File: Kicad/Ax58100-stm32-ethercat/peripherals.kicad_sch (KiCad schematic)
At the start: 32 parts, among them J1 Out_opt, J15 Conn_01x04, J16 Conn_01x02, J17 Conn_01x04, J18 Conn_01x08, J3 In_opt1, J5 In_opt2, J6 DAC, U6 TLP292-4, U7 TLP291-4, U8 TLP292-4

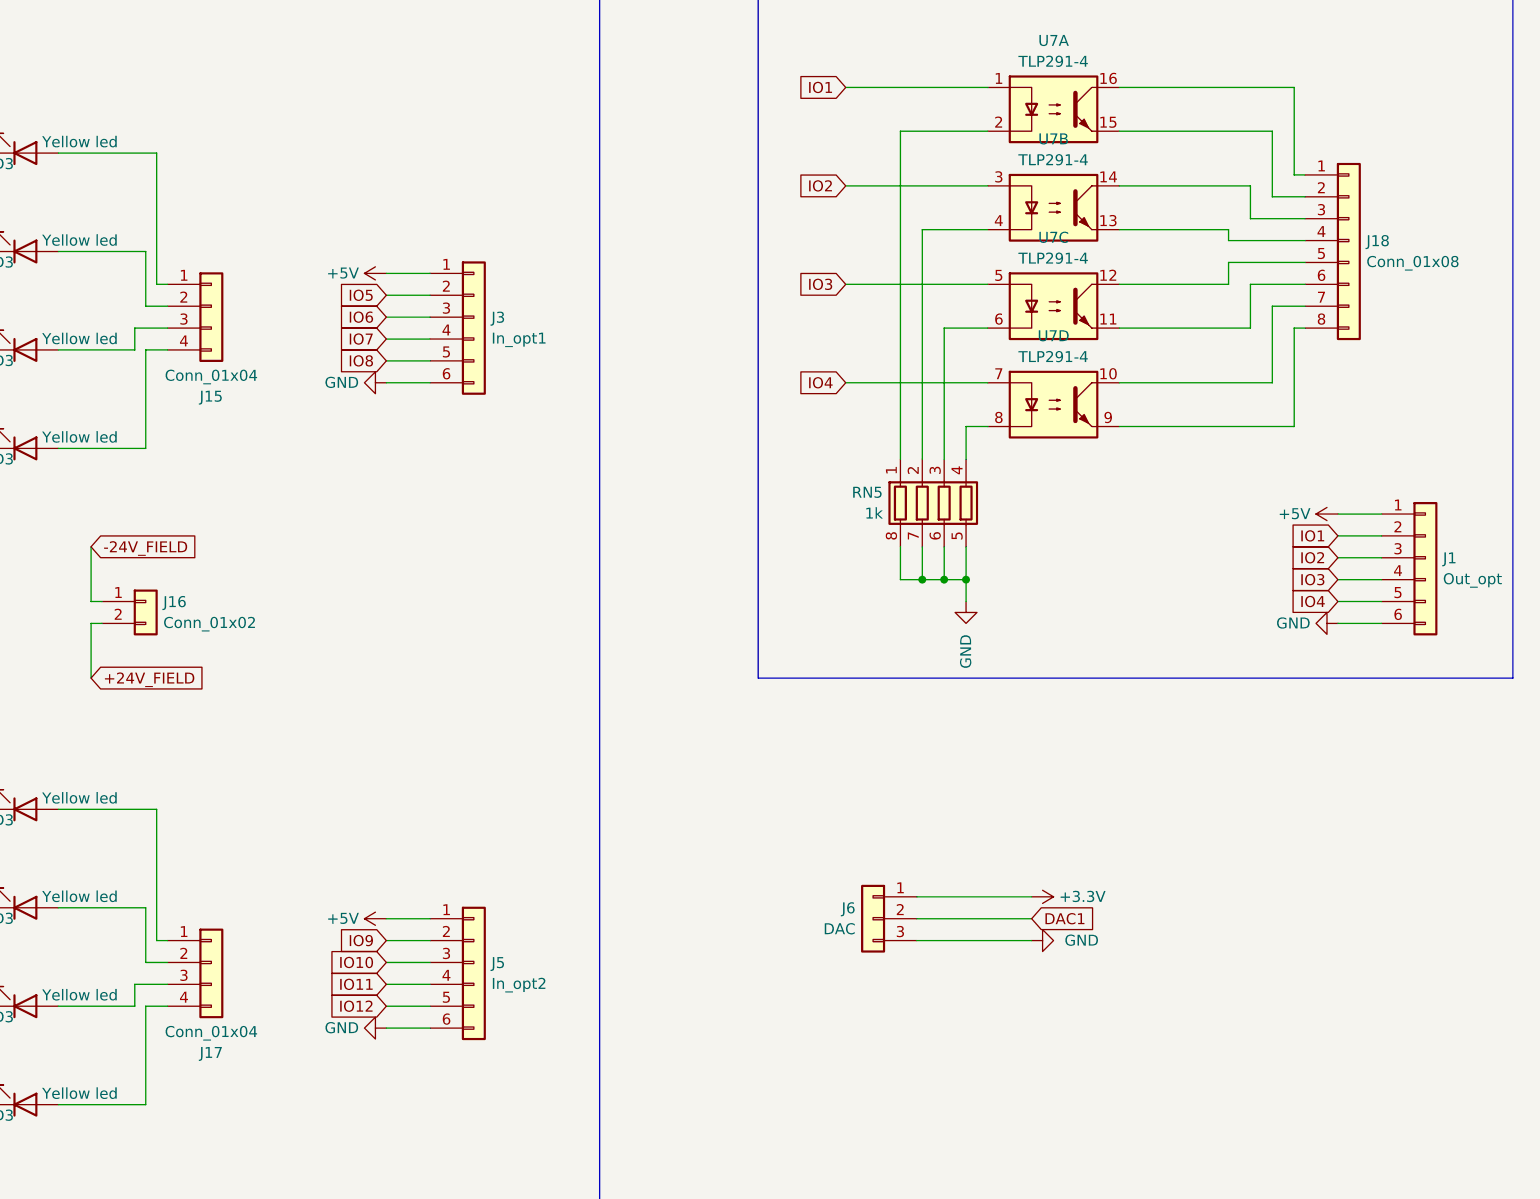
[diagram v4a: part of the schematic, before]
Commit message: Assigned footprints
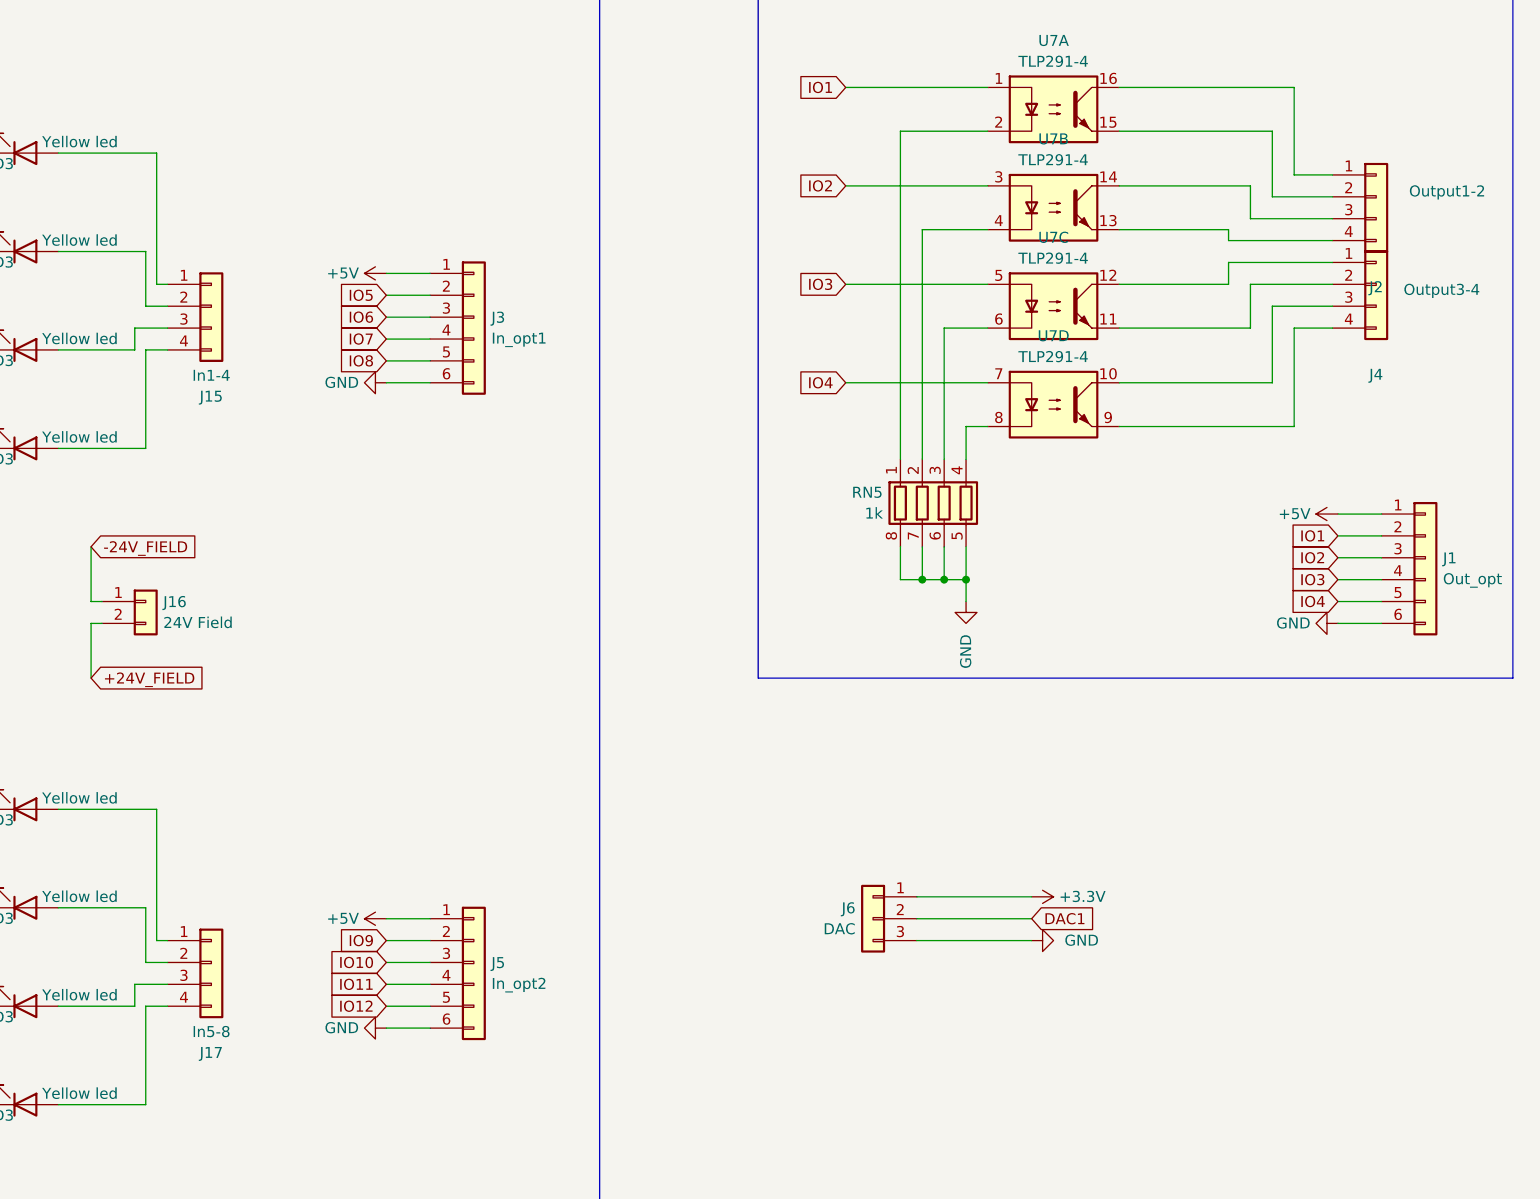
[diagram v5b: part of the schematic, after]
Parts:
- removed J18: Conn_01x08, symbol Connector_Generic:Conn_01x08
- added J2: Output1-2, TerminalBlock:TerminalBlock_bornier-4_P5.08mm, symbol Connector_Generic:Conn_01x04
- added J4: Output3-4, TerminalBlock:TerminalBlock_bornier-4_P5.08mm, symbol Connector_Generic:Conn_01x04
- J1, J3, J5: footprint (none) -> Connector_JST:JST_XH_B6B-XH-A_1x06_P2.50mm_Vertical
- J15: value Conn_01x04 -> In1-4; footprint (none) -> TerminalBlock:TerminalBlock_bornier-4_P5.08mm
- J16: value Conn_01x02 -> 24V Field; footprint (none) -> TerminalBlock:TerminalBlock_bornier-2_P5.08mm
- J17: value Conn_01x04 -> In5-8; footprint (none) -> TerminalBlock:TerminalBlock_bornier-4_P5.08mm
- J6: footprint (none) -> TerminalBlock:TerminalBlock_bornier-3_P5.08mm
- RN1, RN2, RN3, RN4, RN5: footprint (none) -> Resistor_SMD:R_Array_Convex_4x0603
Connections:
- net at U7.10: now also J4.3 (Pin_3)
- net at U7.9: now also J4.4 (Pin_4)
- net at U7.15: now also J2.2 (Pin_2)
- net at U7.16: now also J2.1 (Pin_1)
- net at U7.14: now also J2.3 (Pin_3)
- net at U7.13: now also J2.4 (Pin_4)
- net at U7.12: now also J4.1 (Pin_1)
- net at U7.11: now also J4.2 (Pin_2)
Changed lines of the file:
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@@
     (stroke (width 0) (type default))
   )
-  (wire (pts (xy 252.73 58.42) (xy 246.38 58.42))
+  (wire (pts (xy 255.905 58.42) (xy 246.38 58.42))
     (stroke (width 0) (type default))
   )
@@
     (stroke (width 0) (type default))
   )
-  (wire (pts (xy 251.46 45.72) (xy 252.73 45.72))
+  (wire (pts (xy 251.46 45.72) (xy 255.905 45.72))
     (stroke (width 0) (type default))
   )
@@
     (stroke (width 0) (type default))
   )
-  (wire (pts (xy 243.84 53.34) (xy 252.73 53.34))
+  (wire (pts (xy 243.84 53.34) (xy 255.905 53.34))
     (stroke (width 0) (type default))
   )
@@
     (stroke (width 0) (type default))
   )
-  (wire (pts (xy 243.84 55.88) (xy 252.73 55.88))
+  (wire (pts (xy 243.84 55.88) (xy 255.905 55.88))
     (stroke (width 0) (type default))
   )
@@
     (stroke (width 0) (type default))
   )
-  (wire (pts (xy 251.46 63.5) (xy 252.73 63.5))
+  (wire (pts (xy 251.46 63.5) (xy 255.905 63.5))
     (stroke (width 0) (type default))
   )
@@
     (stroke (width 0) (type default))
   )
-  (wire (pts (xy 248.92 48.26) (xy 252.73 48.26))
+  (wire (pts (xy 248.92 48.26) (xy 255.905 48.26))
     (stroke (width 0) (type default))
   )
@@
     (stroke (width 0) (type default))
   )
-  (wire (pts (xy 252.73 50.8) (xy 246.38 50.8))
+  (wire (pts (xy 255.905 50.8) (xy 246.38 50.8))
     (stroke (width 0) (type default))
   )
@@
     (stroke (width 0) (type default))
   )
-  (wire (pts (xy 248.92 60.96) (xy 252.73 60.96))
+  (wire (pts (xy 248.92 60.96) (xy 255.905 60.96))
     (stroke (width 0) (type default))
   )
@@
       (effects (font (size 1.27 1.27)) (justify left))
     )
-    (property "Footprint" "" (at 90.805 165.1 90)
+    (property "Footprint" "Resistor_SMD:R_Array_Convex_4x0603" (at 90.805 165.1 90)
       (effects (font (size 1.27 1.27)) hide)
     )
@@
       (effects (font (size 1.27 1.27)) (justify left))
     )
-    (property "Footprint" "" (at 202.565 132.08 0)
+    (property "Footprint" "TerminalBlock:TerminalBlock_bornier-3_P5.08mm" (at 202.565 132.08 0)
       (effects (font (size 1.27 1.27)) hide)
     )
@@
       (effects (font (size 1.27 1.27)))
     )
-    (property "Value" "Conn_01x04" (at 125.73 145.2301 0)
-      (effects (font (size 1.27 1.27)))
-    )
-    (property "Footprint" "" (at 125.73 137.16 0)
+    (property "Value" "In5-8" (at 125.73 145.2301 0)
+      (effects (font (size 1.27 1.27)))
+    )
+    (property "Footprint" "TerminalBlock:TerminalBlock_bornier-4_P5.08mm" (at 125.73 137.16 0)
       (effects (font (size 1.27 1.27)) hide)
     )
@@
       (effects (font (size 1.27 1.27)) (justify left))
     )
-    (property "Footprint" "" (at 266.7 90.17 0)
+    (property "Footprint" "Connector_JST:JST_XH_B6B-XH-A_1x06_P2.50mm_Vertical" (at 266.7 90.17 0)
       (effects (font (size 1.27 1.27)) hide)
     )
@@
       (effects (font (size 1.27 1.27)) (justify left))
     )
-    (property "Value" "Conn_01x02" (at 120.142 97.7321 0)
+    (property "Value" "24V Field" (at 120.142 97.7321 0)
       (effects (font (size 1.27 1.27)) (justify left))
     )
-    (property "Footprint" "" (at 118.11 95.25 0)
+    (property "Footprint" "TerminalBlock:TerminalBlock_bornier-2_P5.08mm" (at 118.11 95.25 0)
       (effects (font (size 1.27 1.27)) hide)
     )
@@
       (effects (font (size 1.27 1.27)))
     )
-    (property "Value" "Conn_01x04" (at 125.73 69.0301 0)
-      (effects (font (size 1.27 1.27)))
-    )
-    (property "Footprint" "" (at 125.73 60.96 0)
+    (property "Value" "In1-4" (at 125.73 69.0301 0)
+      (effects (font (size 1.27 1.27)))
+    )
+    (property "Footprint" "TerminalBlock:TerminalBlock_bornier-4_P5.08mm" (at 125.73 60.96 0)
       (effects (font (size 1.27 1.27)) hide)
     )
@@
       (effects (font (size 1.27 1.27)) (justify left))
     )
-    (property "Footprint" "" (at 156.21 62.23 0)
+    (property "Footprint" "Connector_JST:JST_XH_B6B-XH-A_1x06_P2.50mm_Vertical" (at 156.21 62.23 0)
       (effects (font (size 1.27 1.27)) hide)
     )
@@
       (effects (font (size 1.27 1.27)) (justify right))
     )
-    (property "Footprint" "" (at 60.325 90.17 90)
+    (property "Footprint" "Resistor_SMD:R_Array_Convex_4x0603" (at 60.325 90.17 90)
       (effects (font (size 1.27 1.27)) hide)
     )
@@
       (effects (font (size 1.27 1.27)) (justify right))
     )
-    (property "Footprint" "" (at 217.805 83.82 90)
+    (property "Footprint" "Resistor_SMD:R_Array_Convex_4x0603" (at 217.805 83.82 90)
       (effects (font (size 1.27 1.27)) hide)
     )
@@
       (effects (font (size 1.27 1.27)) (justify left))
     )
-    (property "Footprint" "" (at 90.805 88.9 90)
+    (property "Footprint" "Resistor_SMD:R_Array_Convex_4x0603" (at 90.805 88.9 90)
       (effects (font (size 1.27 1.27)) hide)
     )
@@
         (path "/5597aedc-b607-407f-bbfd-31b3b298ecb1/0a376a6c-0f15-42f8-81f6-3a55619be267"
           (reference "#PWR098") (unit 1)
-        )
-      )
-    )
-  )
-  (symbol (lib_id "Connector_Generic:Conn_01x08") (at 257.81 53.34 0) (unit 1)
-    (in_bom yes) (on_board yes) (dnp no) (fields_autoplaced)
-    (property "Reference" "J18" (at 259.842 53.3979 0)
-      (effects (font (size 1.27 1.27)) (justify left))
-    )
-    (property "Value" "Conn_01x08" (at 259.842 55.8221 0)
-      (effects (font (size 1.27 1.27)) (justify left))
-    )
-    (property "Footprint" "" (at 257.81 53.34 0)
-      (effects (font (size 1.27 1.27)) hide)
-    )
-    (property "Datasheet" "~" (at 257.81 53.34 0)
-      (effects (font (size 1.27 1.27)) hide)
-    )
-    (pin "1")
-    (pin "2")
-    (pin "3")
-    (pin "4")
-    (pin "5")
-    (pin "7")
-    (pin "8")
-    (pin "6")
-    (instances
-      (project "Ax58100-stm32-ethercat"
-        (path "/5597aedc-b607-407f-bbfd-31b3b298ecb1/0a376a6c-0f15-42f8-81f6-3a55619be267"
-          (reference "J18") (unit 1)
         )
       )
@@
     )
   )
+  (symbol (lib_id "Connector_Generic:Conn_01x04") (at 260.985 48.26 0) (unit 1)
+    (in_bom yes) (on_board yes) (dnp no)
+    (property "Reference" "J2" (at 260.985 58.7543 0)
+      (effects (font (size 1.27 1.27)))
+    )
+    (property "Value" "Output1-2" (at 269.24 47.625 0)
+      (effects (font (size 1.27 1.27)))
+    )
+    (property "Footprint" "TerminalBlock:TerminalBlock_bornier-4_P5.08mm" (at 260.985 48.26 0)
+      (effects (font (size 1.27 1.27)) hide)
+    )
+    (property "Datasheet" "~" (at 260.985 48.26 0)
+      (effects (font (size 1.27 1.27)) hide)
+    )
+    (pin "1")
+    (pin "2")
+    (pin "3")
+    (pin "4")
+    (instances
+      (project "Ax58100-stm32-ethercat"
+        (path "/5597aedc-b607-407f-bbfd-31b3b298ecb1/0a376a6c-0f15-42f8-81f6-3a55619be267"
+          (reference "J2") (unit 1)
+        )
+      )
+    )
+  )
   (symbol (lib_id "Device:LED") (at 104.14 153.67 0) (mirror x) (unit 1)
     (in_bom yes) (on_board yes) (dnp no)
@@
     )
   )
+  (symbol (lib_id "Connector_Generic:Conn_01x04") (at 260.985 58.42 0) (unit 1)
+    (in_bom yes) (on_board yes) (dnp no)
+    (property "Reference" "J4" (at 260.985 68.9143 0)
+      (effects (font (size 1.27 1.27)))
+    )
+    (property "Value" "Output3-4" (at 268.605 59.055 0)
+      (effects (font (size 1.27 1.27)))
+    )
+    (property "Footprint" "TerminalBlock:TerminalBlock_bornier-4_P5.08mm" (at 260.985 58.42 0)
+      (effects (font (size 1.27 1.27)) hide)
+    )
+    (property "Datasheet" "~" (at 260.985 58.42 0)
+      (effects (font (size 1.27 1.27)) hide)
+    )
+    (pin "1")
+    (pin "2")
+    (pin "3")
+    (pin "4")
+    (instances
+      (project "Ax58100-stm32-ethercat"
+        (path "/5597aedc-b607-407f-bbfd-31b3b298ecb1/0a376a6c-0f15-42f8-81f6-3a55619be267"
+          (reference "J4") (unit 1)
+        )
+      )
+    )
+  )
   (symbol (lib_id "power:GND") (at 146.05 144.78 270) (mirror x) (unit 1)
     (in_bom yes) (on_board yes) (dnp no) (fields_autoplaced)
@@
       (effects (font (size 1.27 1.27)) (justify left))
     )
-    (property "Footprint" "" (at 156.21 137.16 0)
+    (property "Footprint" "Connector_JST:JST_XH_B6B-XH-A_1x06_P2.50mm_Vertical" (at 156.21 137.16 0)
       (effects (font (size 1.27 1.27)) hide)
     )
@@
       (effects (font (size 1.27 1.27)) (justify right))
     )
-    (property "Footprint" "" (at 60.325 166.37 90)
-      (effects (font (size 1.27 1.27)) hide)
-    )
+    (property "Footprint" "Resistor_SMD:R_Array_Convex_4x0603" (at 60.325 166.37 90)
+      (effects (font (size 1.27 1.27)) hide)
+    )

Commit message: First component placement
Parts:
- added D3 (x8): Red led, LED_SMD:LED_0603_1608Metric, symbol Device:LED
- D3: footprint LED_SMD:LED_0805_2012Metric -> LED_SMD:LED_0603_1608Metric
- R46: value 4k7 -> 1k; footprint Resistor_SMD:R_1210_3225Metric -> Resistor_SMD:R_0603_1608Metric
- RN1, RN2: value 1k -> 40k
- RN5: value 1k -> 330
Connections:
- net at U6.4: now also RN4.2 (R2.1); no longer RN4.3 (R3.1)
- net at D3.1 (K), R46.1: now also D3.2 (A) (x8)
- net at D3.2 (A), J17.3 (Pin_3): now also D3.1 (K)
- net at D3.2 (A), J17.2 (Pin_2): now also D3.1 (K)
- net at RN3.1 (R1.1): now also U8.2; no longer U8.8
- net at U8.6: now also RN3.3 (R3.1); no longer RN3.2 (R2.1)
- net at U8.4: now also RN3.2 (R2.1); no longer RN3.3 (R3.1)
- net at RN3.4 (R4.1): now also U8.8; no longer U8.2
- net at U6.8: now also RN4.4 (R4.1); no longer RN4.1 (R1.1)
- net at D3.2 (A), J17.1 (Pin_1): now also D3.1 (K)
- net at D3.2 (A), J17.4 (Pin_4): now also D3.1 (K)
- net at D3.2 (A), J15.1 (Pin_1): now also D3.1 (K)
- net at D3.2 (A), J15.2 (Pin_2): now also D3.1 (K)
- net at D3.2 (A), J15.3 (Pin_3): now also D3.1 (K)
- net at D3.2 (A), J15.4 (Pin_4): now also D3.1 (K)
- net at U6.2: now also RN4.1 (R1.1); no longer RN4.4 (R4.1)
- net at U6.6: now also RN4.3 (R3.1); no longer RN4.2 (R2.1)

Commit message: wip
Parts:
- U4: renamed from U7; value TLP291-4 -> TLP292-4
- renumbered J16 to J11, J6 to J12, J5 to J14, J3 to J17, J1 to J18, J15 to J6, J17 to J7, J2 to J8, J4 to J9, RN5 to RN1, RN4 to RN2, RN1 to RN4, RN2 to RN5, U6 to U5, U8 to U6

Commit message: resistor overhaul
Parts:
- removed RN1: 330, Resistor_SMD:R_Array_Convex_4x0603, symbol Device:R_Pack04
- removed RN2, RN3: 1k, Resistor_SMD:R_Array_Convex_4x0603, symbol Device:R_Pack04
- removed RN4, RN5: 40k, Resistor_SMD:R_Array_Convex_4x0603, symbol Device:R_Pack04
- added R46 (x8): 1k, Resistor_SMD:R_0603_1608Metric, symbol Device:R
- added R59, R60, R61, R62: 330, Resistor_SMD:R_0603_1608Metric, symbol Device:R
- added R63, R64, R65, R66, R67, R68, R69, R70: 39k, Resistor_SMD:R_0603_1608Metric, symbol Device:R
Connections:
- net -24V_FIELD: now also R46.2, R46.2, R46.2, R46.2, R46.2, R46.2, R46.2, R46.2
- net GND: now also R59.2, R60.2, R61.2, R62.2, R63.2, R64.2, R65.2, R66.2, R67.2, R68.2, R69.2, R70.2
- net IO10: now also R68.1
- net IO11: now also R69.1
- net IO12: now also R70.1
- net IO5: now also R63.1
- net IO6: now also R64.1
- net IO7: now also R65.1
- net IO8: now also R66.1
- net IO9: now also R67.1
- net at U5.4: now also R46.1
- net at U6.2: now also R46.1
- net at U4.8: now also R62.1
- net at U5.8: now also R46.1
- net at U4.2: now also R59.1
- net at U6.8: now also R46.1
- net at U5.2: now also R46.1
- net at U4.4: now also R60.1
- net at U4.6: now also R61.1
- net at U5.6: now also R46.1
- net at U6.6: now also R46.1
- net at U6.4: now also R46.1
